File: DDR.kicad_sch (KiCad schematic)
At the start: 1 part, among them U1 IS43LQ32256AL-062BLI

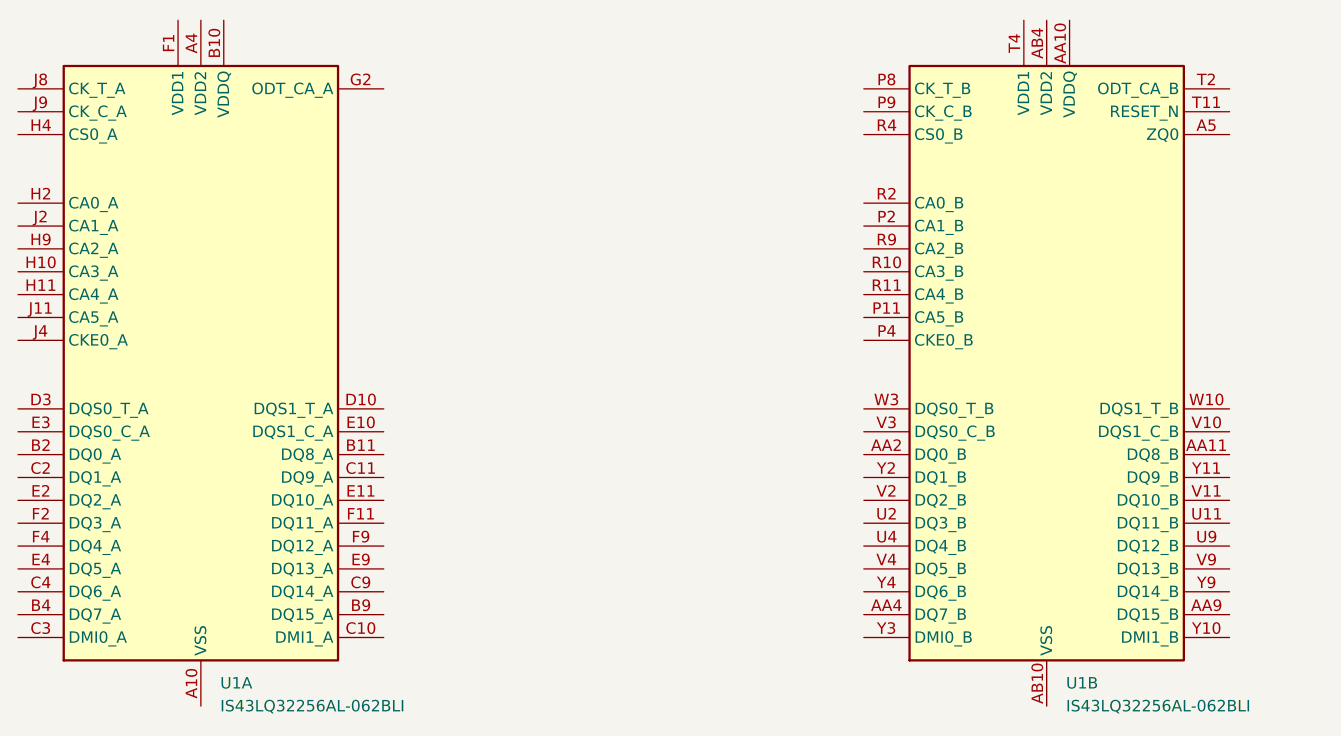
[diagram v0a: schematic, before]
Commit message: расставлены основные блоки и компоненты, подобраны компоненты интерфейса и питания
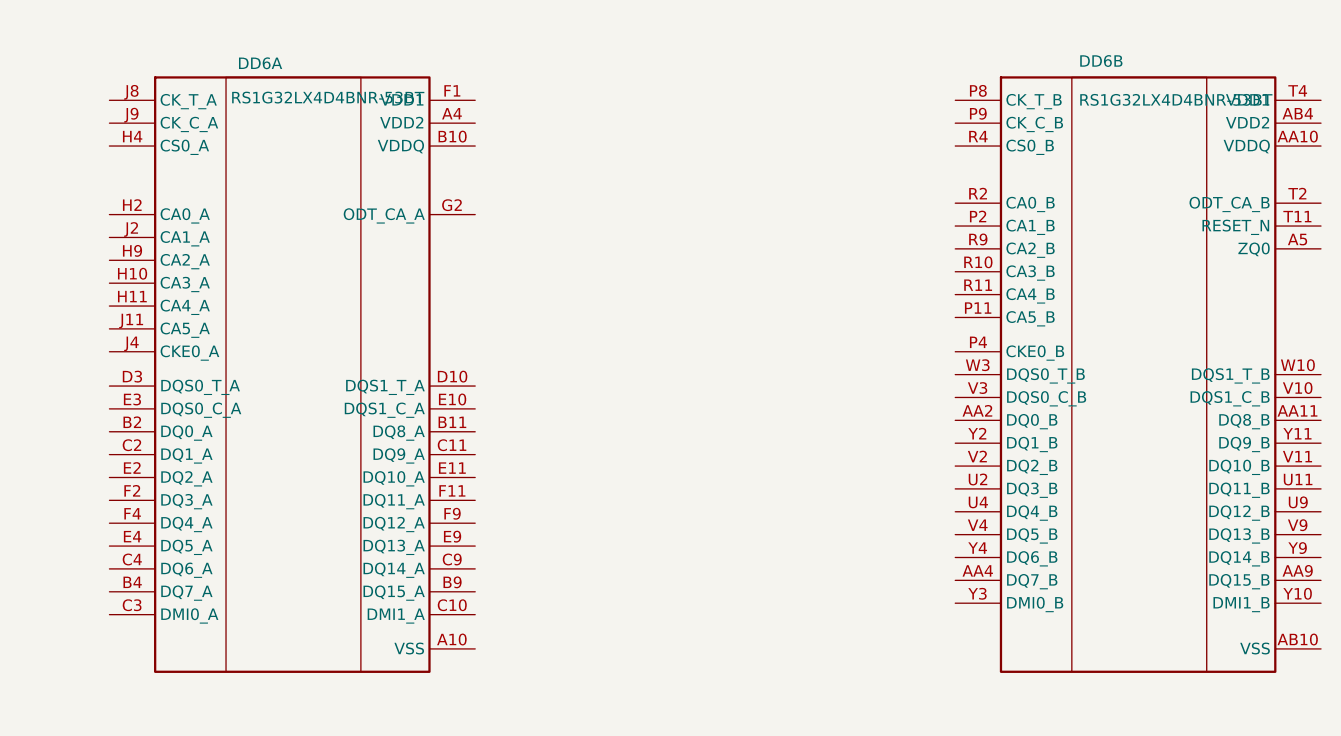
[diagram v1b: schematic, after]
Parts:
- DD6: renamed from U1; value IS43LQ32256AL-062BLI -> RS1G32LX4D4BNR-53BT
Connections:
- net at DD6.AA3 (VDDQ), DD6.AA5 (VDDQ), DD6.AA8 (VDDQ)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: no longer DD6.AA10 (VDDQ)
- net at DD6.AB3 (VSS), DD6.AB5 (VSS), DD6.AB8 (VSS)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: no longer DD6.AB10 (VSS)
- net at DD6.AB9 (VDD2), DD6.N1 (VDD2), DD6.N10 (VDD2)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: no longer DD6.AB4 (VDD2)
- net at DD6.T9 (VDD1), DD6.U1 (VDD1), DD6.U12 (VDD1): no longer DD6.T4 (VDD1)
- net at DD6.A3 (VSS), DD6.C1 (VSS), DD6.C12 (VSS)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: no longer DD6.A10 (VSS)
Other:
- moved on the sheet: DD6A, DD6B
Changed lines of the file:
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@@
 	)
 	(symbol
+		(lib_name "IS43LQ32256AL-062BLI_1")
 		(lib_id "Memory_RAM:IS43LQ32256AL-062BLI")
-		(at 255.27 142.24 0)
+		(at 265.43 143.51 0)
 		(unit 2)
 		(exclude_from_sim no)
@@
 		(on_board yes)
 		(dnp no)
-		(fields_autoplaced yes)
-		(property "Reference" "U1"
-			(at 257.4147 177.8 0)
+		(property "Reference" "DD6"
+			(at 258.826 108.712 0)
 			(effects
 				(font
@@
 			)
 		)
-		(property "Value" "IS43LQ32256AL-062BLI"
-			(at 257.4147 180.34 0)
+		(property "Value" "RS1G32LX4D4BNR-53BT"
+			(at 258.826 113.03 0)
 			(effects
 				(font
@@
 		)
 		(property "Footprint" "Package_BGA:BGA-200_10.0x14.5mm_Layout12x22_P0.80x0.65mm"
-			(at 256.54 190.5 0)
+			(at 266.7 191.77 0)
 			(effects
 				(font
@@
 		)
 		(property "Datasheet" "http://www.issi.com/WW/pdf/43-46LQ32256AL-AL.pdf"
-			(at 252.73 172.72 0)
+			(at 262.89 170.18 0)
 			(effects
 				(font
@@
 		)
 		(property "Description" "256Mx32 bit Low Power Double Data Rate 4X (LPDDR4X) SDRAM, 1600 MHz, Industrial, BGA-200"
-			(at 255.27 142.24 0)
+			(at 265.43 140.97 0)
 			(effects
 				(font
@@
 			(project "Sodimm-force"
 				(path "/b3673bfd-24d8-4789-b63c-c3654dc2bb6e/d150d8cd-7642-4669-b4a1-047329fa175c"
-					(reference "U1")
+					(reference "DD6")
 					(unit 2)
 				)
@@
 	(symbol
 		(lib_id "Memory_RAM:IS43LQ32256AL-062BLI")
-		(at 161.29 142.24 0)
+		(at 171.45 143.51 0)
 		(unit 1)
 		(exclude_from_sim no)
@@
 		(on_board yes)
 		(dnp no)
-		(fields_autoplaced yes)
-		(property "Reference" "U1"
-			(at 163.4347 177.8 0)
+		(property "Reference" "DD6"
+			(at 165.354 108.966 0)
 			(effects
 				(font
@@
 			)
 		)
-		(property "Value" "IS43LQ32256AL-062BLI"
-			(at 163.4347 180.34 0)
+		(property "Value" "RS1G32LX4D4BNR-53BT"
+			(at 164.592 112.776 0)
 			(effects
 				(font
@@
 		)
 		(property "Footprint" "Package_BGA:BGA-200_10.0x14.5mm_Layout12x22_P0.80x0.65mm"
-			(at 162.56 190.5 0)
+			(at 172.72 191.77 0)
 			(effects
 				(font
@@
 		)
 		(property "Datasheet" "http://www.issi.com/WW/pdf/43-46LQ32256AL-AL.pdf"
-			(at 158.75 172.72 0)
+			(at 168.91 170.18 0)
 			(effects
 				(font
@@
 		)
 		(property "Description" "256Mx32 bit Low Power Double Data Rate 4X (LPDDR4X) SDRAM, 1600 MHz, Industrial, BGA-200"
-			(at 161.29 142.24 0)
+			(at 171.45 140.97 0)
 			(effects
 				(font
@@
 			(project "Sodimm-force"
 				(path "/b3673bfd-24d8-4789-b63c-c3654dc2bb6e/d150d8cd-7642-4669-b4a1-047329fa175c"
-					(reference "U1")
+					(reference "DD6")
 					(unit 1)
 				)

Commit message: ddr
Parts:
- removed DD6: RS1G32LX4D4BNR-53BT, Package_BGA:BGA-200_10.0x14.5mm_Layout12x22_P0.80x0.65mm, symbol Memory_RAM:IS43LQ32256AL-062BLI
- added C43, C44, C45, C49, C50, C51, C52, C53, C59, C68: 100nF, Capacitor_SMD:C_0402_1005Metric, symbol Device:C
- added C46, C47, C48, C54, C55, C56, C58, C64, C65, C67: 1uF, Capacitor_SMD:C_0402_1005Metric, symbol Device:C
- added C57, C60: 22uF, Capacitor_SMD:C_0402_1005Metric, symbol Device:C
- added C61, C62, C63: 2.2uF, Capacitor_SMD:C_0402_1005Metric, symbol Device:C
- added DD6: MT53E1G32D2FW-046_AUT_B, LPDDR4:BGA200C65X80P22X12_1500X1000X114N, symbol LPDDR4:MT53E1G32D2FW-046_AUT_B
- added R14: 0R, Resistor_SMD:R_0402_1005Metric, symbol Device:R
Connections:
- new net Earth: C43.2, C44.2, C45.2, C46.2, C47.2, C48.2, C49.2, C50.2, C51.2, C52.2, C53.2, C54.2, C55.2, C56.2, C57.2, C58.2, C59.2, C60.2, C61.2, C62.2, C63.2, C64.2, C65.2, C67.2, C68.2, DD6.A10 (VSS_1__1), DD6.A3 (VSS_1), DD6.AB10 (VSS_4__3), DD6.AB3 (VSS_4), DD6.AB5 (VSS_4__1), DD6.AB8 (VSS_4__2), DD6.C1 (VSS_1__2), DD6.C12 (VSS_1__5), DD6.C5 (VSS_1__3), DD6.C8 (VSS_1__4), DD6.D11 (VSS_1__9), DD6.D2 (VSS_1__6), DD6.D4 (VSS_1__7), DD6.D9 (VSS_1__8), DD6.E1 (VSS_1__10), DD6.E12 (VSS_1__13), DD6.E5 (VSS_1__11), DD6.E8 (VSS_1__12), DD6.G1 (VSS_1__14), DD6.G10 (VSS_2__3), DD6.G12 (VSS_2__4), DD6.G3 (VSS_2), DD6.G5 (VSS_2__1), DD6.G8 (VSS_2__2), DD6.J1 (VSS_2__5), DD6.J10 (VSS_2__7), DD6.J12 (VSS_2__8), DD6.J3 (VSS_2__6), DD6.K11 (VSS_2__12), DD6.K2 (VSS_2__9), DD6.K4 (VSS_2__10), DD6.K9 (VSS_2__11), DD6.N11 (VSS_3__2), DD6.N2 (VSS_2__13), DD6.N4 (VSS_3), DD6.N9 (VSS_3__1), DD6.P1 (VSS_3__3), DD6.P10 (VSS_3__5), DD6.P12 (VSS_3__6), DD6.P3 (VSS_3__4), DD6.T1 (VSS_3__7), DD6.T10 (VSS_3__11), DD6.T12 (VSS_3__12), DD6.T3 (VSS_3__8), DD6.T5 (VSS_3__9), DD6.T8 (VSS_3__10), DD6.V1 (VSS_3__13), DD6.V12 (VSS_4__5), DD6.V5 (VSS_3__14), DD6.V8 (VSS_4__4), DD6.W11 (VSS_4__9), DD6.W2 (VSS_4__6), DD6.W4 (VSS_4__7), DD6.W9 (VSS_4__8), DD6.Y1 (VSS_4__10), DD6.Y12 (VSS_4__13), DD6.Y5 (VSS_4__11), DD6.Y8 (VSS_4__12)
- new net SA0: DD6.H2 (CA0_A)
- new net SA1: DD6.J2 (CA1_A)
- new net SA2: DD6.H9 (CA2_A)
- new net SA3: DD6.H10 (CA3_A)
- new net SA4: DD6.H11 (CA4_A)
- new net SA5: DD6.J11 (CA5_A)
- new net SCKE0: DD6.J4 (CKE0_A)
- new net VCC-DRAM: C43.1, C44.1, C45.1, C46.1, C47.1, C48.1, C49.1, C50.1, C51.1, C52.1, C53.1, C54.1, C55.1, C56.1, C60.1, C61.1, C62.1, C63.1, C64.1, C65.1, DD6.A4 (VDD2_1), DD6.A9 (VDD2_1__1), DD6.AA10 (VDDQ_2__3), DD6.AA3 (VDDQ_2), DD6.AA5 (VDDQ_2__1), DD6.AA8 (VDDQ_2__2), DD6.AB4 (VDD2_2), DD6.AB9 (VDD2_2__1), DD6.B10 (VDDQ_1__3), DD6.B3 (VDDQ_1), DD6.B5 (VDDQ_1__1), DD6.B8 (VDDQ_1__2), DD6.D1 (VDDQ_1__4), DD6.D12 (VDDQ_1__7), DD6.D5 (VDDQ_1__5), DD6.D8 (VDDQ_1__6), DD6.F1 (VDD1), DD6.F10 (VDDQ_1__9), DD6.F3 (VDDQ_1__8), DD6.F5 (VDD2_1__2), DD6.F8 (VDD2_1__3), DD6.H1 (VDD2_1__4), DD6.H12 (VDD2_1__7), DD6.H5 (VDD2_1__5), DD6.H8 (VDD2_1__6), DD6.K1 (VDD2_1__8), DD6.K10 (VDD2_1__10), DD6.K12 (VDD2_1__11), DD6.K3 (VDD2_1__9), DD6.N1 (VDD2_1__12), DD6.N10 (VDD2_1__14), DD6.N12 (VDD2_2__2), DD6.N3 (VDD2_1__13), DD6.R1 (VDD2_2__3), DD6.R12 (VDD2_2__6), DD6.R5 (VDD2_2__4), DD6.R8 (VDD2_2__5), DD6.U10 (VDDQ_1__11), DD6.U3 (VDDQ_1__10), DD6.U5 (VDD2_2__7), DD6.U8 (VDD2_2__8), DD6.W1 (VDDQ_1__12), DD6.W12 (VDDQ_2__4), DD6.W5 (VDDQ_1__13), DD6.W8 (VDDQ_1__14)
- new net VDD18-LPDDR: C57.1, C58.1, C59.1, C67.1, C68.1, DD6.F12 (VDD1__1), DD6.G4 (VDD1__2), DD6.G9 (VDD1__3), DD6.T4 (VDD1__4), DD6.T9 (VDD1__5), DD6.U1 (VDD1__6), DD6.U12 (VDD1__7)

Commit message: Доработка DDR, питание
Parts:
- added R15: 240R, Resistor_SMD:R_0402_1005Metric, symbol Device:R
- added R16, R17: 100K, Resistor_SMD:R_0402_1005Metric, symbol Device:R
- R14: value 0R -> 240R
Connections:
- net Earth: now also R14.1, R15.1
- net SA0: now also DD6.R2 (CA0_B)
- net SA1: now also DD6.P2 (CA1_B)
- net SA2: now also DD6.R9 (CA2_B)
- net SA3: now also DD6.R10 (CA3_B)
- net SA4: now also DD6.R11 (CA4_B)
- net SA5: now also DD6.P11 (CA5_B)
- net SCKE0: now also DD6.P4 (CKE0_B)
- net VCC-DRAM: now also R16.1, R17.1
- net at R14.2: now also DD6.A5 (ZQ0)
- net at DD6.A8 (ZQ1): now also R15.2
- net SDQ5: now reaches DD6.AA11 (DQ8_B)
- net SDQ13: now reaches DD6.AA2 (DQ0_B)
- net SDQ15: now reaches DD6.AA4 (DQ7_B)
- net SDQ6: now reaches DD6.AA9 (DQ15_B)
- net SDQ27: now reaches DD6.B11 (DQ8_A)
- net SDQ22: now reaches DD6.B2 (DQ0_A)
- net SDQ19: now reaches DD6.B4 (DQ7_A)
- net SDQ30: now reaches DD6.B9 (DQ15_A)
- net SDQM3: now reaches DD6.C10 (DMI1_A)
- net SDQ28: now reaches DD6.C11 (DQ9_A)
- net SDQ20: now reaches DD6.C2 (DQ1_A)
- net SDQM2: now reaches DD6.C3 (DMI0_A)
- net SDQ16: now reaches DD6.C4 (DQ6_A)
- net SDQ24: now reaches DD6.C9 (DQ14_A)
- net SDQS3P: now reaches DD6.D10 (DQS1_T_A)
- net SDQS2P: now reaches DD6.D3 (DQS0_T_A)
- net SDQS3N: now reaches DD6.E10 (DQS1_C_A)
- net SDQ31: now reaches DD6.E11 (DQ10_A)
- net SDQ23: now reaches DD6.E2 (DQ2_A)
- net SDQS2N: now reaches DD6.E3 (DQS0_C_A)
- net SDQ18: now reaches DD6.E4 (DQ5_A)
- net SDQ25: now reaches DD6.E9 (DQ13_A)
- net SDQ29: now reaches DD6.F11 (DQ11_A)
- net SDQ21: now reaches DD6.F2 (DQ3_A)
- net SDQ17: now reaches DD6.F4 (DQ4_A)
- net SDQ26: now reaches DD6.F9 (DQ12_A)
- net at DD6.G2 (ODT_CA_A): now also R17.2
- net SCS1: now reaches DD6.H3 (CS1_A)
- net SCS1: now also DD6.R3 (CS1_B)
- net SCS0: now reaches DD6.H4 (CS0_A)
- net SCS0: now also DD6.R4 (CS0_B)
- net SCKE1: now reaches DD6.J5 (SCKE1)
- net SCKE1: now also DD6.P5 (SCKE1)
- net SCKP: now reaches DD6.J8 (CK_T_A)
- net SCKP: now also DD6.P8 (CK_T_B)
- net SCKN: now reaches DD6.J9 (CK_C_A)
- net SCKN: now also DD6.P9 (CK_C_B)
- net SRST: now reaches DD6.T11 (~{RESET})
- net at DD6.T2 (ODT_CA_B): now also R16.2
- net SDQ0: now reaches DD6.U11 (DQ11_B)
- net SDQ12: now reaches DD6.U2 (DQ3_B)
- net SDQ14: now reaches DD6.U4 (DQ4_B)
- net SDQ1: now reaches DD6.U9 (DQ12_B)
- net SDQSON: now reaches DD6.V10 (DQS1_C_B)
- net SDQ2: now reaches DD6.V11 (DQ10_B)
- net SDQ9: now reaches DD6.V2 (DQ2_B)
- net SDQS1N: now reaches DD6.V3 (DQS0_C_B)
- net SDQ11: now reaches DD6.V4 (DQ5_B)
- net SDQ3: now reaches DD6.V9 (DQ13_B)
- net SDQS0P: now reaches DD6.W10 (DQS1_T_B)
- net SDQS1P: now reaches DD6.W3 (DQS0_T_B)
- net SDQMO: now reaches DD6.Y10 (DMI1_B)
- net SDQ7: now reaches DD6.Y11 (DQ9_B)
- net SDQ10: now reaches DD6.Y2 (DQ1_B)
- net SDQM1: now reaches DD6.Y3 (DMI0_B)
- net SDQ8: now reaches DD6.Y4 (DQ6_B)
- net SDQ4: now reaches DD6.Y9 (DQ14_B)
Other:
- moved on the sheet: C43, C44, C45, C46, C47, C48, C49, C50, C51, C52, C53, C54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

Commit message: Схема закончена, часть компонентов расставлена на плате
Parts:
- renumbered C60 to C64, C61 to C65, C62 to C66, C63 to C67, C64 to C68, C65 to C69, C52 to C70, C43 to C71, C44 to C72, C45 to C73, C46 to C74, C47 to C75, C48 to C76, C49 to C77, C50 to C78, C51 to C79, C53 to C80, C54 to C81, C55 to C82, C56 to C83, C57 to C84, C58 to C85, C59 to C86, C67 to C87, C68 to C88, R15 to R32, R14 to R33, R17 to R34, R16 to R35
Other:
- note added: "LPDDR4"

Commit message: Пытаюсь сделать трассировку DDК
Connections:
- net SDQMO renamed SDQM0
- net SDQSON renamed SDQS0N
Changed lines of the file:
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@@
 	(wire
 		(pts
-			(xy 109.22 143.51) (xy 106.68 143.51)
-		)
-		(stroke
-			(width 0)
-			(type default)
-		)
-	)
-	(wire
-		(pts
 			(xy 288.29 130.81) (xy 302.26 130.81)
 		)
@@
 	(wire
 		(pts
+			(xy 109.22 143.51) (xy 106.68 143.51)
+		)
+		(stroke
+			(width 0)
+			(type default)
+		)
+	)
+	(wire
+		(pts
 			(xy 135.89 236.22) (xy 142.24 236.22)
 		)
@@
 		)
 	)
-	(global_label "SDQMO"
+	(global_label "SDQM0"
 		(shape input)
 		(at 152.4 130.81 0)
@@
 		)
 	)
-	(global_label "SDQSON"
+	(global_label "SDQS0N"
 		(shape input)
 		(at 152.4 181.61 0)
@@
 		)
 		(property "Intersheetrefs" "${INTERSHEET_REFS}"
-			(at 161.8561 181.61 0)
+			(at 162.9447 181.61 0)
 			(effects
 				(font
